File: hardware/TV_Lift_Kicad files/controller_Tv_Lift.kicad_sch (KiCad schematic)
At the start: 96 parts, among them J1 socket LAN8720a, J10 CONN_IR_OUT, J11 DRY CONTACT UP DOWN, J12 DRY CONTACT, J2 POWER 24V, J3 CAN_bus, J4 ENCODER, J5 ENCODER_POWER, J6 CONN_RS232, J7 M1 LIMIT UP DOWN, J8 Signal PWR, J9 MOTOR_OUT, Q1 2N3904, SW1 UP, SW2 DOWN, SW3 STOP, U1 MAX3232, U10 VNH5019A-E, U2 TSOP32S40F, U3 SN65HVD230, U4 ESP32-WROOM-32, U5 LM2596S-5, U6 AMS1117-3.3, U7 PC817, U8 PC817, U9 NCS1S1205SC

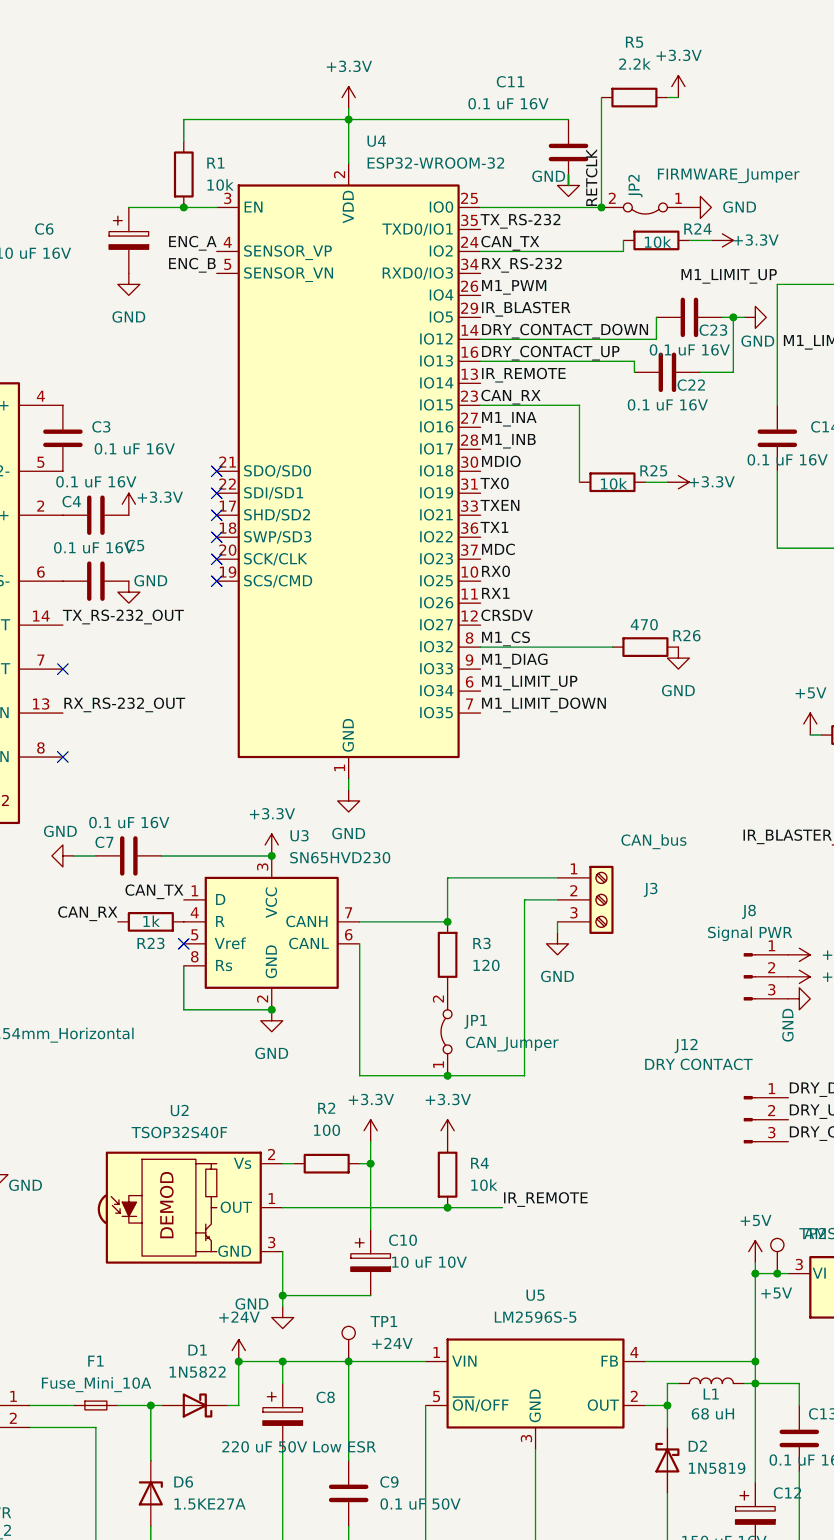
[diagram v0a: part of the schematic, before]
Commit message: change inpit diod
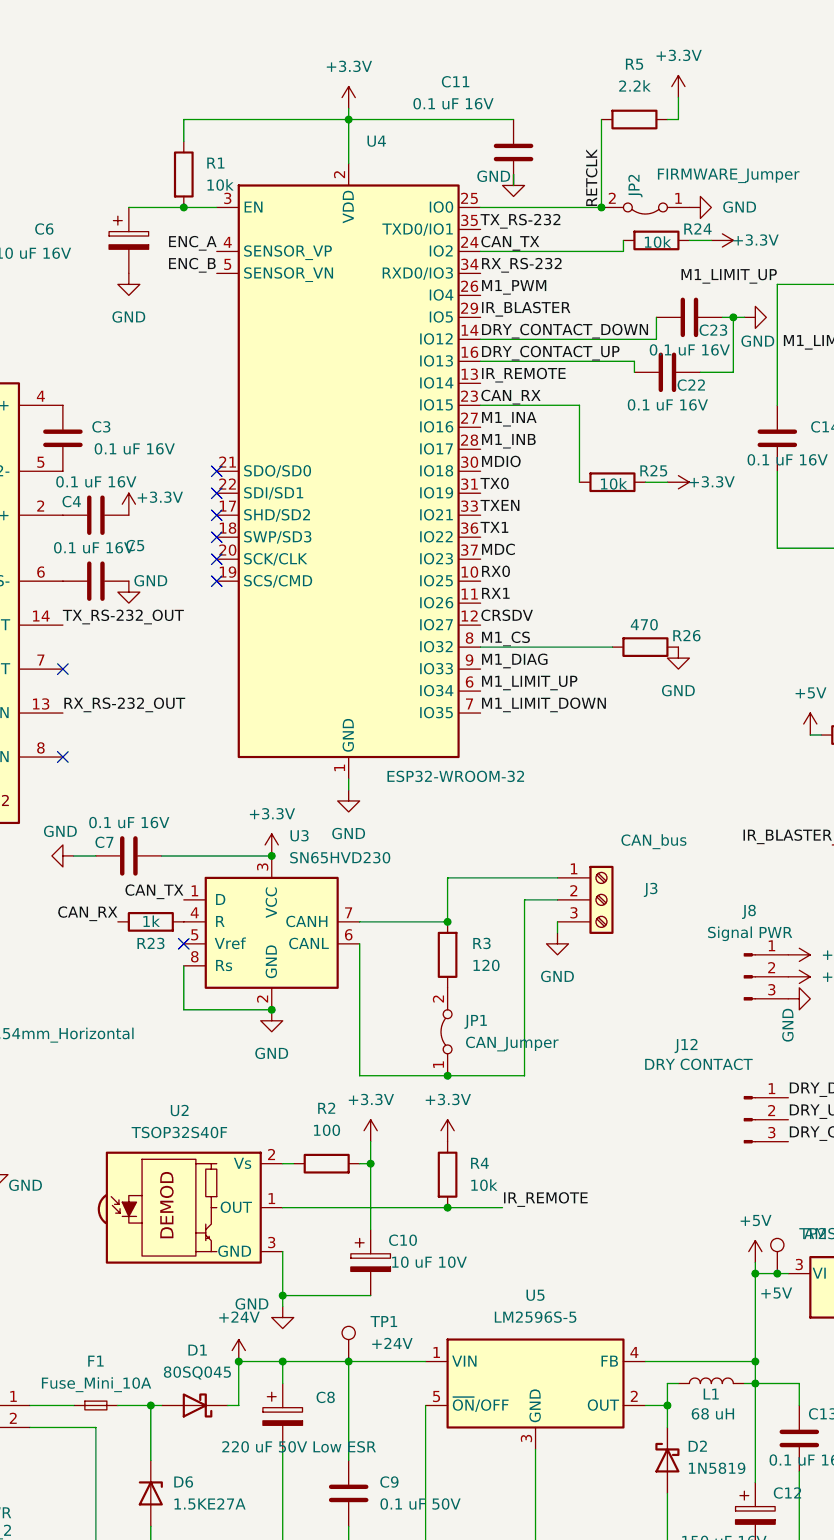
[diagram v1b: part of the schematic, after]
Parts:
- D1: value 1N5822 -> 80SQ045
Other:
- moved on the sheet: C11, R5
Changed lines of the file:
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@@
 	)
 	(junction
+		(at 129.54 31.75)
+		(diameter 0)
+		(color 0 0 0 0)
+	)
+	(junction
 		(at 147.32 167.64)
 		(diameter 0)
@@
 	)
 	(junction
-		(at 129.54 31.75)
-		(diameter 0)
-		(color 0 0 0 0)
-	)
-	(junction
 		(at 236.22 99.06)
 		(diameter 0)
@@
 	(wire
 		(pts
+			(xy 138.43 21.59) (xy 138.43 19.05)
+		)
+		(stroke
+			(width 0)
+			(type default)
+		)
+	)
+	(wire
+		(pts
 			(xy 144.78 44.45) (xy 146.05 44.45)
 		)
@@
 	(wire
 		(pts
-			(xy 129.54 19.05) (xy 129.54 31.75)
+			(xy 129.54 21.59) (xy 129.54 31.75)
 		)
 		(stroke
@@
 	(wire
 		(pts
-			(xy 137.16 19.05) (xy 138.43 19.05)
+			(xy 137.16 21.59) (xy 138.43 21.59)
 		)
 		(stroke
@@
 	(wire
 		(pts
-			(xy 125.73 21.59) (xy 100.33 21.59)
+			(xy 119.38 21.59) (xy 100.33 21.59)
 		)
 		(stroke
@@
 	(wire
 		(pts
-			(xy 125.73 27.94) (xy 125.73 29.21)
+			(xy 119.38 27.94) (xy 119.38 29.21)
 		)
 		(stroke
@@
 		(in_pos_files yes)
 		(dnp no)
-		(fields_autoplaced yes)
 		(property "Reference" "U4"
 			(at 102.3494 24.13 0)
@@
 		)
 		(property "Value" "ESP32-WROOM-32"
-			(at 102.3494 26.67 0)
+			(at 104.648 97.536 0)
 			(show_name no)
 			(do_not_autoplace no)
@@
 			)
 		)
-		(property "Value" "1N5822"
+		(property "Value" "80SQ045"
 			(at 82.8675 166.37 0)
 			(show_name no)
@@
 	(symbol
 		(lib_id "Device:C")
-		(at 125.73 25.4 0)
+		(at 119.38 25.4 0)
 		(unit 1)
 		(body_style 1)
@@
 		(dnp no)
 		(property "Reference" "C11"
-			(at 117.348 17.272 0)
+			(at 110.998 17.272 0)
 			(show_name no)
 			(do_not_autoplace no)
@@
 		)
 		(property "Value" "0.1 uF 16V"
-			(at 114.046 19.812 0)
+			(at 107.696 19.812 0)
 			(show_name no)
 			(do_not_autoplace no)
@@
 		)
 		(property "Footprint" "Capacitor_SMD:C_0805_2012Metric"
-			(at 126.6952 29.21 0)
+			(at 120.3452 29.21 0)
 			(hide yes)
 			(show_name no)
@@
 		)
 		(property "Datasheet" ""
-			(at 125.73 25.4 0)
+			(at 119.38 25.4 0)
 			(hide yes)
 			(show_name no)
@@
 		)
 		(property "Description" ""
-			(at 125.73 25.4 0)
+			(at 119.38 25.4 0)
 			(show_name no)
 			(do_not_autoplace no)
@@
 		(lib_name "GND_11")
 		(lib_id "power:GND")
-		(at 125.73 27.94 0)
+		(at 119.38 27.94 0)
 		(unit 1)
 		(body_style 1)
@@
 		(dnp no)
 		(property "Reference" "#PWR025"
-			(at 125.73 34.29 0)
+			(at 119.38 34.29 0)
 			(hide yes)
 			(show_name no)
@@
 		)
 		(property "Value" "GND"
-			(at 123.444 28.194 0)
+			(at 117.094 28.194 0)
 			(show_name no)
 			(do_not_autoplace no)
@@
 		)
 		(property "Footprint" ""
-			(at 125.73 27.94 0)
+			(at 119.38 27.94 0)
 			(hide yes)
 			(show_name no)
@@
 		)
 		(property "Datasheet" ""
-			(at 125.73 27.94 0)
+			(at 119.38 27.94 0)
 			(hide yes)
 			(show_name no)
@@
 		)
 		(property "Description" ""
-			(at 125.73 27.94 0)
+			(at 119.38 27.94 0)
 			(show_name no)
 			(do_not_autoplace no)
@@
 	(symbol
 		(lib_id "Device:R")
-		(at 133.35 19.05 270)
+		(at 133.35 21.59 270)
 		(unit 1)
 		(body_style 1)
@@
 		(fields_autoplaced yes)
 		(property "Reference" "R5"
-			(at 133.35 12.7 90)
+			(at 133.35 15.24 90)
 			(show_name no)
 			(do_not_autoplace no)
@@
 		)
 		(property "Value" "2.2k"
-			(at 133.35 15.24 90)
+			(at 133.35 17.78 90)
 			(show_name no)
 			(do_not_autoplace no)
@@
 		)
 		(property "Footprint" "Resistor_SMD:R_0805_2012Metric"
-			(at 133.35 17.272 90)
+			(at 133.35 19.812 90)
 			(hide yes)
 			(show_name no)
@@
 		)
 		(property "Datasheet" ""
-			(at 133.35 19.05 0)
+			(at 133.35 21.59 0)
 			(hide yes)
 			(show_name no)
@@
 		)
 		(property "Description" ""
-			(at 133.35 19.05 0)
+			(at 133.35 21.59 0)
 			(show_name no)
 			(do_not_autoplace no)

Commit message: add button reset
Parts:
- added SW4: Reset, Button_Switch_THT:SW_PUSH_6mm, symbol Switch:SW_Push
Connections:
- net GND: now also SW4.1
- net at C6.1, R1.2, U4.3 (EN): now also SW4.2
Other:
- moved on the sheet: C6
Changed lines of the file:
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@@
 	)
 	(junction
+		(at 81.28 31.75)
+		(diameter 0)
+		(color 0 0 0 0)
+	)
+	(junction
 		(at 173.99 48.26)
 		(diameter 0)
@@
 	)
 	(junction
+		(at 67.31 31.75)
+		(diameter 0)
+		(color 0 0 0 0)
+	)
+	(junction
 		(at 91.44 124.46)
 		(diameter 0)
@@
 	)
 	(junction
+		(at 67.31 39.37)
+		(diameter 0)
+		(color 0 0 0 0)
+	)
+	(junction
 		(at 200.66 144.78)
 		(diameter 0)
@@
 	)
 	(junction
-		(at 81.28 31.75)
-		(diameter 0)
-		(color 0 0 0 0)
-	)
-	(junction
 		(at 236.22 99.06)
 		(diameter 0)
@@
 	(wire
 		(pts
+			(xy 57.15 31.75) (xy 57.15 39.37)
+		)
+		(stroke
+			(width 0)
+			(type default)
+		)
+	)
+	(wire
+		(pts
 			(xy 134.62 165.1) (xy 147.32 165.1)
 		)
@@
 	(wire
 		(pts
-			(xy 74.93 31.75) (xy 81.28 31.75)
+			(xy 67.31 31.75) (xy 81.28 31.75)
 		)
 		(stroke
@@
 	(wire
 		(pts
+			(xy 57.15 39.37) (xy 67.31 39.37)
+		)
+		(stroke
+			(width 0)
+			(type default)
+		)
+	)
+	(wire
+		(pts
 			(xy 77.47 170.18) (xy 77.47 176.53)
 		)
@@
 	)
 	(symbol
+		(lib_id "Switch:SW_Push")
+		(at 62.23 31.75 0)
+		(unit 1)
+		(body_style 1)
+		(exclude_from_sim no)
+		(in_bom yes)
+		(on_board yes)
+		(in_pos_files yes)
+		(dnp no)
+		(fields_autoplaced yes)
+		(property "Reference" "SW4"
+			(at 62.23 24.13 0)
+			(show_name no)
+			(do_not_autoplace no)
+			(effects
+				(font
+					(size 1.27 1.27)
+				)
+			)
+		)
+		(property "Value" "Reset"
+			(at 62.23 26.67 0)
+			(show_name no)
+			(do_not_autoplace no)
+			(effects
+				(font
+					(size 1.27 1.27)
+				)
+			)
+		)
+		(property "Footprint" "Button_Switch_THT:SW_PUSH_6mm"
+			(at 62.23 26.67 0)
+			(hide yes)
+			(show_name no)
+			(do_not_autoplace no)
+			(effects
+				(font
+					(size 1.27 1.27)
+				)
+			)
+		)
+		(property "Datasheet" ""
+			(at 62.23 26.67 0)
+			(hide yes)
+			(show_name no)
+			(do_not_autoplace no)
+			(effects
+				(font
+					(size 1.27 1.27)
+				)
+			)
+		)
+		(property "Description" "Push button switch, generic, two pins"
+			(at 62.23 31.75 0)
+			(hide yes)
+			(show_name no)
+			(do_not_autoplace no)
+			(effects
+				(font
+					(size 1.27 1.27)
+				)
+			)
+		)
+		(pin "2"
+		)
+		(pin "1"
+		)
+		(instances
+			(project "controller_Tv_Lift"
+				(path "/906b0219-e8e2-4a64-a5ea-d0350d472c53"
+					(reference "SW4")
+					(unit 1)
+				)
+			)
+		)
+	)
+	(symbol
 		(lib_id "Device:R")
 		(at 207.01 33.02 0)
@@
 	(symbol
 		(lib_id "Device:C_Polarized")
-		(at 74.93 35.56 0)
+		(at 67.31 35.56 0)
 		(unit 1)
 		(body_style 1)
@@
 		(dnp no)
 		(property "Reference" "C6"
-			(at 64.008 34.29 0)
+			(at 71.882 37.084 0)
 			(show_name no)
 			(do_not_autoplace no)
@@
 		)
 		(property "Value" "10 uF 16V"
-			(at 59.436 37.084 0)
+			(at 69.85 33.274 0)
 			(show_name no)
 			(do_not_autoplace no)
@@
 		)
 		(property "Footprint" "Capacitor_THT:CP_Radial_D5.0mm_P2.00mm"
-			(at 75.8952 39.37 0)
+			(at 68.2752 39.37 0)
 			(hide yes)
 			(show_name no)
@@
 		)
 		(property "Datasheet" ""
-			(at 74.93 35.56 0)
+			(at 67.31 35.56 0)
 			(hide yes)
 			(show_name no)
@@
 		)
 		(property "Description" ""
-			(at 74.93 35.56 0)
+			(at 67.31 35.56 0)
 			(show_name no)
 			(do_not_autoplace no)
@@
 		(lib_name "GND_20")
 		(lib_id "power:GND")
-		(at 74.93 39.37 0)
+		(at 67.31 39.37 0)
 		(unit 1)
 		(body_style 1)
@@
 		(fields_autoplaced yes)
 		(property "Reference" "#PWR010"
-			(at 74.93 45.72 0)
+			(at 67.31 45.72 0)
 			(hide yes)
 			(show_name no)
@@
 		)
 		(property "Value" "GND"
-			(at 74.93 44.45 0)
+			(at 67.31 44.45 0)
 			(show_name no)
 			(do_not_autoplace no)
@@
 		)
 		(property "Footprint" ""
-			(at 74.93 39.37 0)
+			(at 67.31 39.37 0)
 			(hide yes)
 			(show_name no)
@@
 		)
 		(property "Datasheet" ""
-			(at 74.93 39.37 0)
+			(at 67.31 39.37 0)
 			(hide yes)
 			(show_name no)
@@
 		)
 		(property "Description" ""
-			(at 74.93 39.37 0)
+			(at 67.31 39.37 0)
 			(show_name no)
 			(do_not_autoplace no)

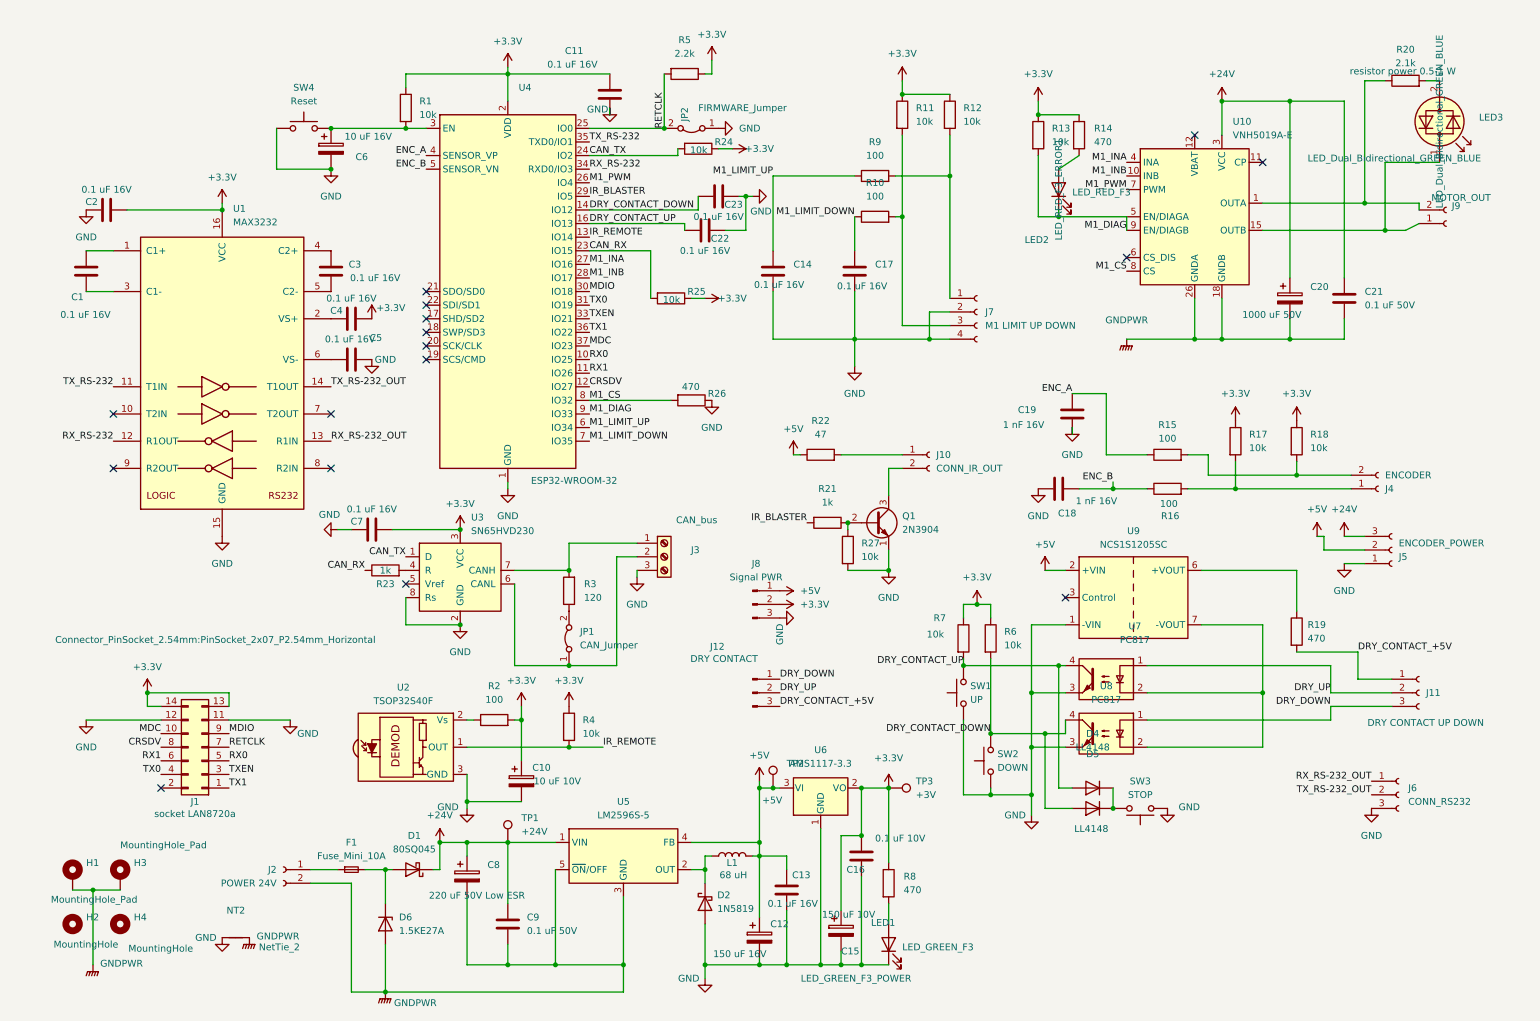
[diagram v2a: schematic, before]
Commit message: change diod suspressor
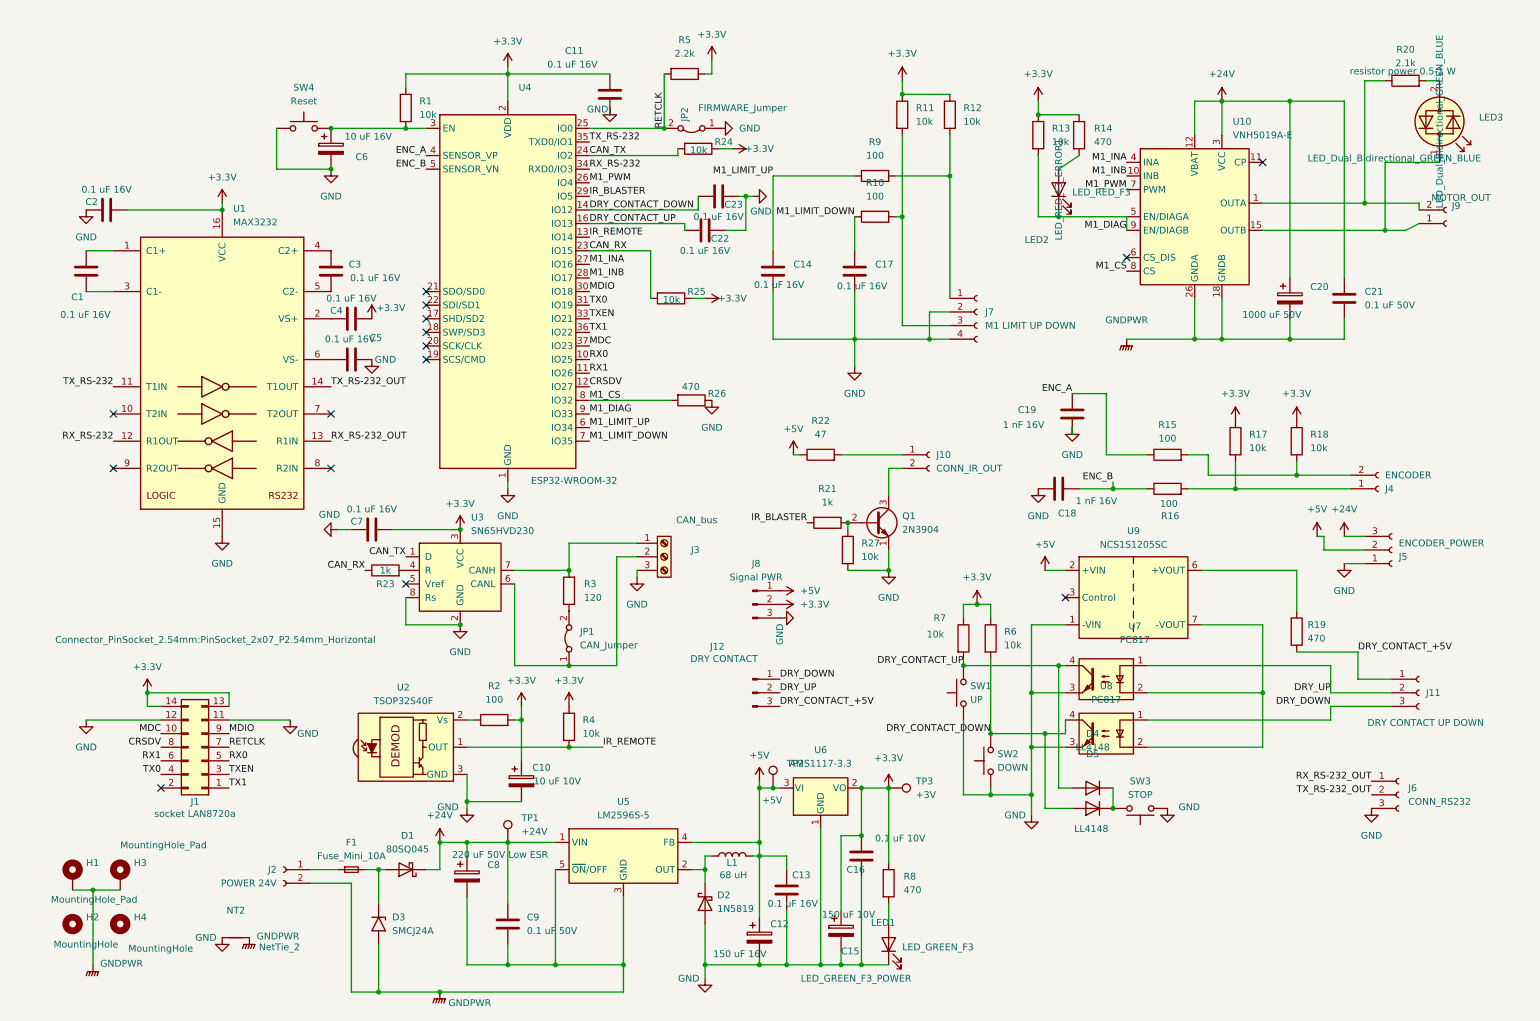
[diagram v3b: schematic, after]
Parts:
- removed D6: 1.5KE27A, Diode_THT:D_DO-201AD_P15.24mm_Horizontal, symbol Diode:PTVS26VZ1USK
- added D3: SMCJ24A, Diode_SMD:D_SMC, symbol Diode:1.5SMCxxA
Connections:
- net +24V: now also U10.12 (VBAT)
- net GNDPWR: now also D3.2 (A2)
- net at D1.2 (A), F1.2: now also D3.1 (A1)
- no-connect marks 16 -> 15
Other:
- moved on the sheet: D1

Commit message: add prodactions file
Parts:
- D1: value 80SQ045 -> 20SQ045
- D3: value SMCJ24A -> SMCJ26A
- J2: footprint Connector_Phoenix_MC:PhoenixContact_MC_1,5_2-G-3.5_1x02_P3.50mm_Horizontal -> Connector_Phoenix_MC_HighVoltage:PhoenixContact_MC_1,5_2-G-5.08_1x02_P5.08mm_Horizontal
- LED2, LED3: footprint LED_THT:LED_D3.0mm_Horizontal_O1.27mm_Z2.0mm -> LED_THT:LED_D3.0mm_Horizontal_O1.27mm_Z6.0mm
- R20: value 2.1k -> 2.4k
- R22: footprint Resistor_SMD:R_0805_2012Metric -> Resistor_SMD:R_1206_3216Metric
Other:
- moved on the sheet: J1, NT2, R26
